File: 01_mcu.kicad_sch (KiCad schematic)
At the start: 3 parts, among them J2 UART, J3 SWD

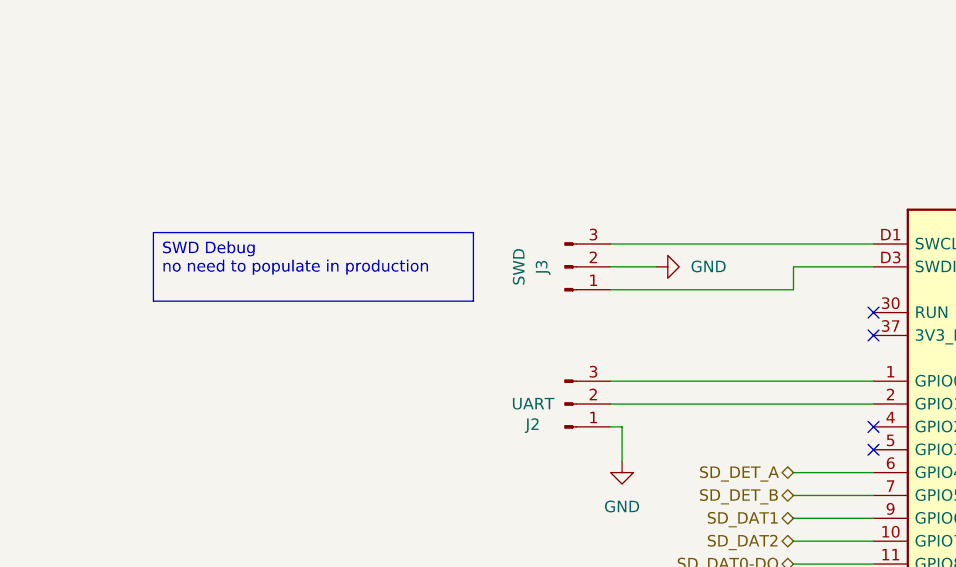
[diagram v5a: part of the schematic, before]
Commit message: v2: finished schematics, start routing
The schematics for v2 should be mostly finished by now.
The new on/off button is ready and tested with a breadboard setup.
It now uses two FETs for a self-holding circuit for turning the
device on and off. To reach a safe logic level for Pico 2, a
2.7V Zener diode is used together with a pull-down for E9 affected
RP2350 revisions.
Besides, most pull-up resistors are 10k now to keep the BoM
smaller.

Routing started with a major redesign.
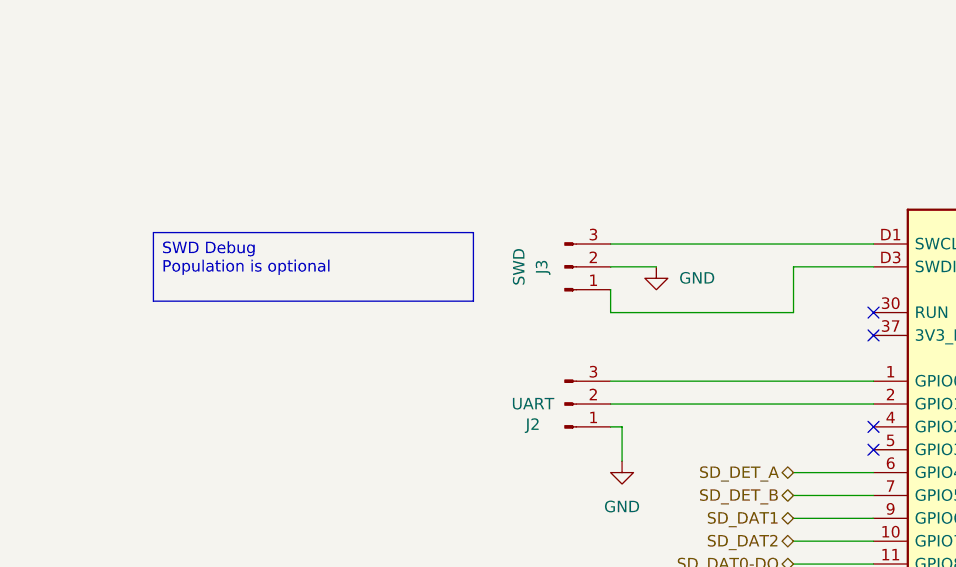
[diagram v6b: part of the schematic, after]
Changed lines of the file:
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@@
 		)
 	)
-	(text_box "SWD Debug\nno need to populate in production"
+	(text_box "SWD Debug\nPopulation is optional"
 		(exclude_from_sim no)
 		(at 55.88 66.04 0)
@@
 		(stroke
 			(width 0)
-			(type default)
+			(type solid)
 		)
 		(fill
@@
 	(wire
 		(pts
+			(xy 106.68 74.93) (xy 106.68 72.39)
+		)
+		(stroke
+			(width 0)
+			(type default)
+		)
+	)
+	(wire
+		(pts
 			(xy 181.61 115.57) (xy 189.23 115.57)
 		)
@@
 	(wire
 		(pts
-			(xy 127 72.39) (xy 106.68 72.39)
+			(xy 127 74.93) (xy 106.68 74.93)
 		)
 		(stroke
@@
 	(wire
 		(pts
-			(xy 127 69.85) (xy 127 72.39)
+			(xy 127 69.85) (xy 127 74.93)
 		)
 		(stroke
@@
 	(symbol
 		(lib_id "power:GND")
-		(at 111.76 69.85 90)
+		(at 111.76 69.85 0)
 		(unit 1)
 		(exclude_from_sim no)
@@
 		(fields_autoplaced yes)
 		(property "Reference" "#PWR022"
-			(at 118.11 69.85 0)
+			(at 111.76 76.2 0)
 			(effects
 				(font
@@
 		)
 		(property "Value" "GND"
-			(at 115.57 69.8499 90)
-			(effects
-				(font
-					(size 1.27 1.27)
-				)
-				(justify right)
-			)
-		)
+			(at 114.3 71.1199 0)
+			(effects
+				(font
+					(size 1.27 1.27)
+				)
+				(justify left)
+			)
+		)

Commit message: Reworked v2 routing
- some general improvements
- reworked component numbering
- routed and tuned differential pair (USB)
- added stiching vias and improved ground fills
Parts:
- renumbered J2 to J4, J3 to J5
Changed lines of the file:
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@@
-	(wire
-		(pts
-			(xy 106.68 74.93) (xy 106.68 72.39)
-		)
-		(stroke
-			(width 0)
-			(type default)
-		)
-	)
 	(wire
 		(pts
@@
 	(wire
 		(pts
-			(xy 127 74.93) (xy 106.68 74.93)
+			(xy 110.49 76.2) (xy 110.49 69.85)
 		)
 		(stroke
@@
 	(wire
 		(pts
-			(xy 135.89 69.85) (xy 127 69.85)
+			(xy 135.89 69.85) (xy 121.92 69.85)
 		)
 		(stroke
@@
 	(wire
 		(pts
+			(xy 106.68 72.39) (xy 121.92 72.39)
+		)
+		(stroke
+			(width 0)
+			(type default)
+		)
+	)
+	(wire
+		(pts
 			(xy 181.61 113.03) (xy 189.23 113.03)
 		)
@@
 	(wire
 		(pts
+			(xy 110.49 69.85) (xy 106.68 69.85)
+		)
+		(stroke
+			(width 0)
+			(type default)
+		)
+	)
+	(wire
+		(pts
 			(xy 127 115.57) (xy 135.89 115.57)
 		)
@@
 	(wire
 		(pts
-			(xy 111.76 69.85) (xy 106.68 69.85)
-		)
-		(stroke
-			(width 0)
-			(type default)
-		)
-	)
-	(wire
-		(pts
 			(xy 127 92.71) (xy 135.89 92.71)
 		)
@@
 	(wire
 		(pts
-			(xy 127 69.85) (xy 127 74.93)
+			(xy 121.92 69.85) (xy 121.92 72.39)
 		)
 		(stroke
@@
 		(on_board yes)
 		(dnp no)
-		(property "Reference" "J3"
-			(at 99.06 69.85 90)
+		(property "Reference" "J5"
+			(at 97.79 71.12 0)
 			(effects
 				(font
@@
 		)
 		(property "Value" "SWD"
-			(at 96.52 69.85 90)
+			(at 98.044 68.834 0)
 			(effects
 				(font
@@
 			(project "ZEReader-Pico"
 				(path "/ec954637-2a8b-4662-b4a1-f88107f11cb0/8ebc337b-62e9-431a-9c7d-4f5ee75e8f92"
-					(reference "J3")
+					(reference "J5")
 					(unit 1)
 				)
@@
 		(on_board yes)
 		(dnp no)
-		(property "Reference" "J2"
+		(property "Reference" "J4"
 			(at 98.044 87.376 0)
 			(effects
@@
 			(project ""
 				(path "/ec954637-2a8b-4662-b4a1-f88107f11cb0/8ebc337b-62e9-431a-9c7d-4f5ee75e8f92"
-					(reference "J2")
+					(reference "J4")
 					(unit 1)
 				)
@@
 	(symbol
 		(lib_id "power:GND")
-		(at 111.76 69.85 0)
+		(at 110.49 76.2 0)
 		(unit 1)
 		(exclude_from_sim no)
@@
 		(fields_autoplaced yes)
 		(property "Reference" "#PWR022"
-			(at 111.76 76.2 0)
+			(at 110.49 82.55 0)
 			(effects
 				(font
@@
 		)
 		(property "Value" "GND"
-			(at 114.3 71.1199 0)
+			(at 113.03 77.4699 0)
 			(effects
 				(font
@@
 		)
 		(property "Footprint" ""
-			(at 111.76 69.85 0)
+			(at 110.49 76.2 0)
 			(effects
 				(font
@@
 		)
 		(property "Datasheet" ""
-			(at 111.76 69.85 0)
+			(at 110.49 76.2 0)
 			(effects
 				(font
@@
 		)
 		(property "Description" "Power symbol creates a global label with name \"GND\" , ground"
-			(at 111.76 69.85 0)
-			(effects
-				(font
+			(at 110.49 76.2 0)
+			(effects
+				(font
